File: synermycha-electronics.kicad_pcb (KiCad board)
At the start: 4 copper layers, 50 x 75 mm, 159 parts, among them J1 BATT, J11 USB_B_Micro, J12 Conn_01x05, J13 Conn_01x05, J14 Conn_01x05, J15 Conn_01x05, J16 Conn_01x05, J17 Conn_01x03, J2 Conn_01x02, J3 Conn_01x02, J4 USB_B_Micro, J5 ESP_01, J6 A1250WV-S-4P, Q1 IRLML9301TRPBF, Q2 BC847, Q3 BC847, Q4 BC847, Q5 IRLML2060TRPBF, Q6 IRLML2060TRPBF, Q7 IRLML9301TRPBF, SW1 DTSM32N, SW2 DTSM32N, SW3 DTSM32N, SW4 DTSM32N, U1 LM1117LDX, U12 MPU-9250, U13 STM32F446RETx, U14 STM14_SW, U2 LM1117LDX, U3 LM1117LDX, U4 DRV8835, U5 LM1117LDX, U8 CP2102N-A01-GQFN28, U9 TS5A3167DBVR, Y1 16Mhz, 8pF

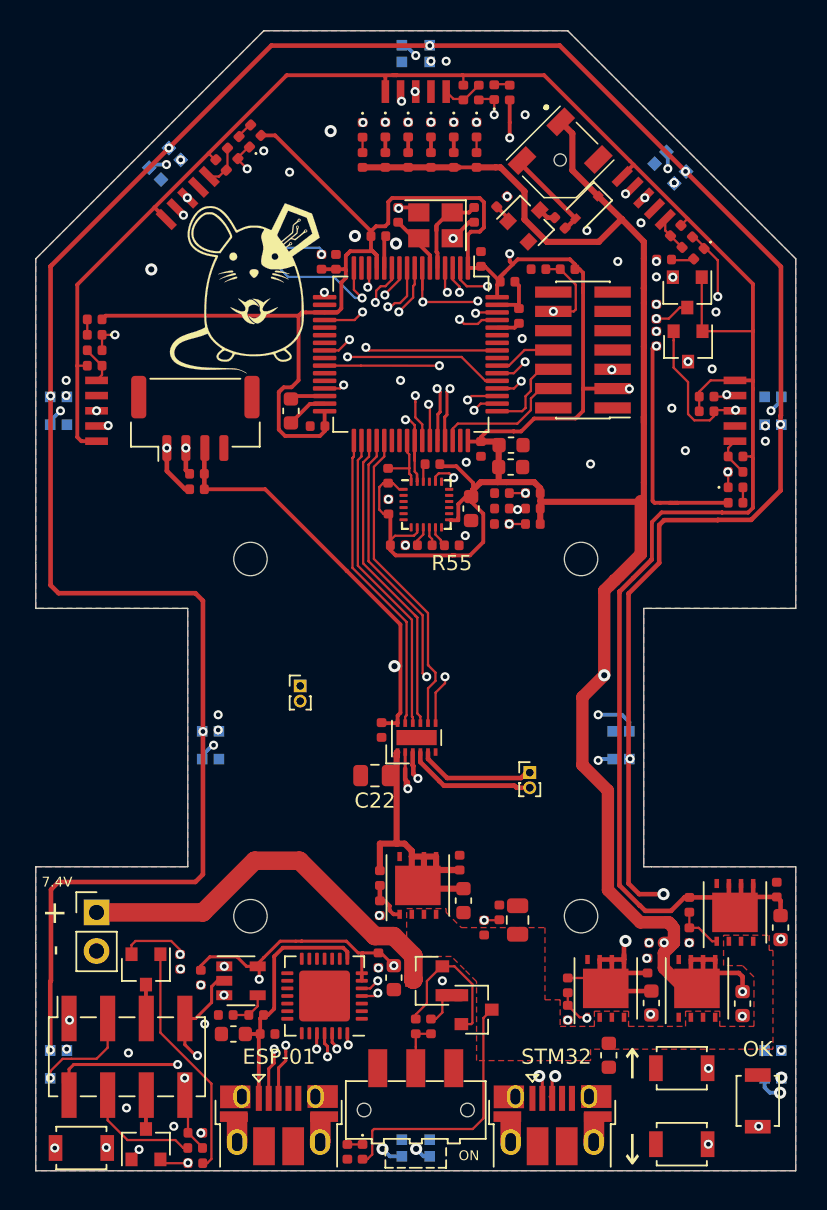
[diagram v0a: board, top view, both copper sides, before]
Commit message: Changes in graphics, added capacitors, changes in xshut
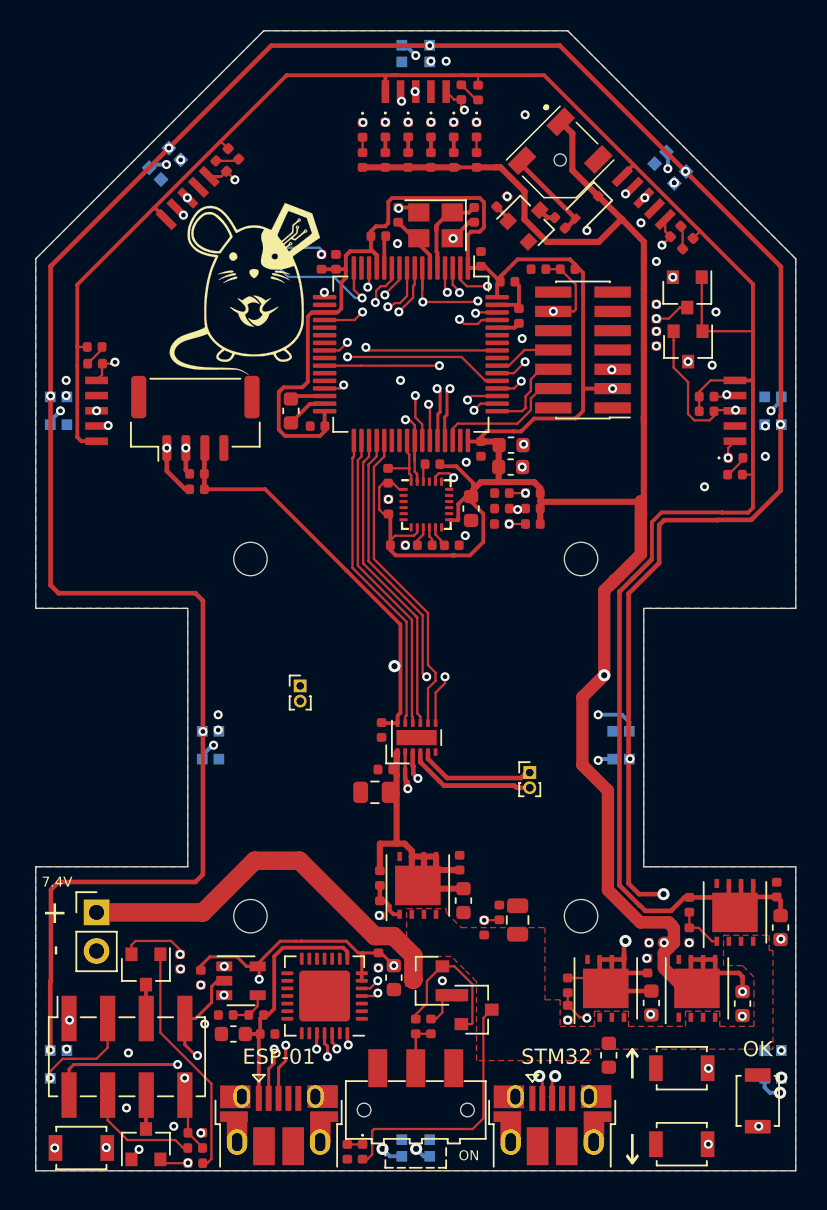
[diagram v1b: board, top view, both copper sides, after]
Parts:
- removed R36, R37, R38, R39, R40, R47, R48: 1K, Resistor_SMD:R_0402_1005Metric
- removed R41, R44, R45: 47K, Resistor_SMD:R_0402_1005Metric
- removed the REF** at (27.8, 137.8)
- added C23: 0.1uF, Capacitor_SMD:C_0402_1005Metric, F.Cu at (35.0, 171.6)
- R42, R43: value 47K -> 140R
- R46, R49, R50: value 1K -> 140R
- moved D18 2.20 mm to (24.2, 131.9)
- moved D15 2.16 mm to (40.0, 127.0)
- moved R49 2.15 mm to (25.0, 131.1), turned to 135 degrees
- moved D19 2.12 mm to (54.1, 136.2), turned to 45 degrees
- moved R46 2.08 mm to (41.1, 127.1), turned to 90 degrees
- moved D16 1.94 mm to (58.0, 151.1)
- moved D17 1.90 mm to (15.9, 144.9)
- moved R50 1.88 mm to (54.9, 137.0), turned to 45 degrees
- moved R43 1.23 mm to (15.9, 143.8)
- moved R42 1.20 mm to (58.0, 152.2)
- moved C22 1.10 mm to (34.3, 173.1)
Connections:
- D15 pad 1: Net-(D15-Pad1) -> /Distance Sensors/VL53L0x_~XSHUT[1]
- D16 pad 1: Net-(D16-Pad1) -> /Distance Sensors/VL53L0x_~XSHUT[2]
- D17 pad 1: Net-(D17-Pad1) -> /Distance Sensors/VL53L0x_~XSHUT[3]
- D18 pad 1: Net-(D18-Pad1) -> /Distance Sensors/VL53L0x_~XSHUT[4]
- D19 pad 1: Net-(D19-Pad1) -> /Distance Sensors/VL53L0x_~XSHUT[5]
- R42 pad 2: /Distance Sensors/VL53L0x_~XSHUT[2] -> Net-(D16-Pad2)
- R43 pad 2: /Distance Sensors/VL53L0x_~XSHUT[3] -> Net-(D17-Pad2)
- R46 pad 2: +3V3 -> +2V8
- R49 pad 2: +3V3 -> +2V8
- R50 pad 2: +3V3 -> +2V8
- U13 pad 2: Net-(D19-Pad1) -> /Distance Sensors/VL53L0x_~XSHUT[5]
- U13 pad 20: Net-(D18-Pad1) -> /Distance Sensors/VL53L0x_~XSHUT[4]
- U13 pad 24: Net-(D17-Pad1) -> /Distance Sensors/VL53L0x_~XSHUT[3]
- U13 pad 3: Net-(D15-Pad1) -> /Distance Sensors/VL53L0x_~XSHUT[1]
- U13 pad 54: Net-(D16-Pad1) -> /Distance Sensors/VL53L0x_~XSHUT[2]
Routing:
- net +3V3: track 391.5 -> 341.8 mm, vias 13 -> 11
- net Net-(D19-Pad1): track 23.0 -> 0.00 mm, vias 2 -> 0
- net Net-(D16-Pad1): track 20.8 -> 0.00 mm, vias 2 -> 0
- net /Distance Sensors/VL53L0x_~XSHUT[4]: track 2.82 -> 22.4 mm, vias 0 -> 2
- net Net-(D17-Pad1): track 19.4 -> 0.00 mm, vias 2 -> 0
- net Net-(D18-Pad1): track 19.1 -> 0.00 mm, vias 2 -> 0
- net /Distance Sensors/VL53L0x_~XSHUT[2]: track 3.16 -> 20.6 mm, vias 0 -> 2
- net /Distance Sensors/VL53L0x_~XSHUT[3]: track 3.06 -> 20.1 mm, vias 0 -> 2
- net Net-(D15-Pad1): track 16.5 -> 0.00 mm, vias 2 -> 0
- net /Distance Sensors/VL53L0x_~XSHUT[5]: track 2.42 -> 17.4 mm, vias 0 -> 2
- net /Distance Sensors/VL53L0x_~XSHUT[1]: track 2.80 -> 17.6 mm, vias 0 -> 2
- net +6V: track 27.0 -> 27.6 mm
- net Net-(D16-Pad2): track 1.02 -> 1.55 mm
- net GND: vias 48 -> 41

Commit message: Cosmetics update
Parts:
- added REF**: mocowanie_silników, mocowanie_silników:mocowanie_silników, F.Cu at (36.9, 168.5)
- moved R5 0.56 mm to (55.5, 180.8)
- moved R6 0.50 mm to (55.5, 182.5)
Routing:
- net +3V3: track 341.8 -> 328.7 mm, vias 11 -> 10
- net Net-(J3-Pad2): track 17.8 -> 13.2 mm
- net +5V: track 255.4 -> 258.2 mm
- net /Distance Sensors/VL53L0x_~XSHUT[1]: track 17.6 -> 18.3 mm
- net Net-(R5-Pad2): track 3.20 -> 2.58 mm
- net +2V8: track 154.7 -> 155.3 mm
- net GND: vias 41 -> 40
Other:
- outline, holes or cut-outs redrawn

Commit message: Estetics
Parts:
- added REF**: hole_0.8mm, holes:hole_0.8mm, F.Cu at (27.8, 137.8)
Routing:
- net +3V3: track 328.7 -> 338.5 mm, vias 10 -> 9
- net Net-(J3-Pad2): track 13.2 -> 17.8 mm
- net GND: track 14.8 -> 16.7 mm, vias 40 -> 38
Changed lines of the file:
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@@
   (general
     (thickness 1.6)
-    (drawings 50)
-    (tracks 1605)
+    (drawings 49)
+    (tracks 1610)
     (zones 0)
-    (modules 150)
+    (modules 151)
     (nets 105)
   )
@@
     (2 In2.Cu signal)
     (31 B.Cu signal)
-    (32 B.Adhes user)
-    (33 F.Adhes user)
-    (34 B.Paste user)
-    (35 F.Paste user)
+    (32 B.Adhes user hide)
+    (33 F.Adhes user hide)
+    (34 B.Paste user hide)
+    (35 F.Paste user hide)
     (36 B.SilkS user)
     (37 F.SilkS user)
@@
     (39 F.Mask user)
     (40 Dwgs.User user)
-    (41 Cmts.User user)
-    (42 Eco1.User user)
-    (43 Eco2.User user)
+    (41 Cmts.User user hide)
+    (42 Eco1.User user hide)
+    (43 Eco2.User user hide)
     (44 Edge.Cuts user)
-    (45 Margin user)
-    (46 B.CrtYd user)
-    (47 F.CrtYd user)
-    (48 B.Fab user)
-    (49 F.Fab user)
+    (45 Margin user hide)
+    (46 B.CrtYd user hide)
+    (47 F.CrtYd user hide)
+    (48 B.Fab user hide)
+    (49 F.Fab user hide)
   )
   (setup
-    (last_trace_width 0.25)
+    (last_trace_width 0.3048)
     (user_trace_width 0.1524)
     (user_trace_width 0.2032)
@@
     (add_net "Net-(R55-Pad2)")
   )
+  (module holes:hole_0.8mm (layer F.Cu)
+    (at 27.75 137.85)
+    (fp_text reference REF** (at 0 -2.5) (layer F.SilkS) hide
+      (effects (font (size 1 1) (thickness 0.15)))
+    )
+    (fp_text value hole_0.8mm (at 0 -0.5) (layer F.Fab)
+      (effects (font (size 1 1) (thickness 0.15)))
+    )
+    (pad "" np_thru_hole circle (at 0 0) (size 0.8 0.8) (drill 0.762) (layers *.Cu *.Mask))
+  )
   (module mocowanie_silników:mocowanie_silników (layer F.Cu)
     (at 36.9 168.5 180)
-    (fp_text reference REF** (at 16 5.75) (layer F.SilkS)
+    (fp_text reference REF** (at 16 5.75) (layer F.SilkS) hide
       (effects (font (size 1 1) (thickness 0.15)))
     )
@@
       (rotate (xyz -90 0 90))
     )
+    (model ${KIPRJMOD}/3D_models/FTSH-107-01-L-DV-K-TR.stp
+      (offset (xyz 0 0 0.5))
+      (scale (xyz 1 1 1))
+      (rotate (xyz -90 0 90))
+    )
   )
   (module Capacitor_SMD:C_0402_1005Metric (layer F.Cu)
@@
   (gr_arc (start 13 197) (end 12 197) (angle -90) (layer Edge.Cuts) (width 0.05))
   (gr_arc (start 61 197) (end 61 198) (angle -90) (layer Edge.Cuts) (width 0.05))
-  (dimension 75 (width 0.15) (layer Dwgs.User)
-    (gr_text "75,000 mm" (at -73.3 160.5 270) (layer Dwgs.User)
-      (effects (font (size 1 1) (thickness 0.15)))
-    )
-    (feature1 (pts (xy 38 198) (xy -72.586421 198)))
-    (feature2 (pts (xy 38 123) (xy -72.586421 123)))
-    (crossbar (pts (xy -72 123) (xy -72 198)))
-    (arrow1a (pts (xy -72 198) (xy -72.586421 196.873496)))
-    (arrow1b (pts (xy -72 198) (xy -71.413579 196.873496)))
-    (arrow2a (pts (xy -72 123) (xy -72.586421 124.126504)))
-    (arrow2b (pts (xy -72 123) (xy -71.413579 124.126504)))
-  )
   (dimension 17 (width 0.15) (layer Dwgs.User)
     (gr_text "17,000 mm" (at -11.3 169.5 90) (layer Dwgs.User)
@@
     (effects (font (size 0.65 0.65) (thickness 0.15)))
   )
-  (gr_text 7.4V (at 13.4 179) (layer F.SilkS)
+  (gr_text 7.4V (at 16 179) (layer F.SilkS)
     (effects (font (size 0.65 0.65) (thickness 0.15)))
   )
@@
   (via (at 52.451 187.706) (size 0.6) (drill 0.3) (layers F.Cu B.Cu) (net 1))
   (via (at 52.197 184.023) (size 0.6) (drill 0.3) (layers F.Cu B.Cu) (net 1))
-  (via (at 34.6 181.2) (size 0.6) (drill 0.3) (layers F.Cu B.Cu) (net 1))
   (via (at 47 188.085) (size 0.6) (drill 0.3) (layers F.Cu B.Cu) (net 1))
-  (via (at 34.544 184.658) (size 0.6) (drill 0.3) (layers F.Cu B.Cu) (net 1))
   (via (at 49.9 145.3) (size 0.6) (drill 0.3) (layers F.Cu B.Cu) (net 1))
   (via (at 24.384 186.436) (size 0.6) (drill 0.3) (layers F.Cu B.Cu) (net 1))
@@
   (via (at 44.196 128.524) (size 0.6) (drill 0.3) (layers F.Cu B.Cu) (net 1))
   (via (at 35.8 137) (size 0.6) (drill 0.3) (layers F.Cu B.Cu) (net 1))
+  (segment (start 34.544 184.664482) (end 34.544 184.635) (width 0.1524) (layer F.Cu) (net 1))
+  (segment (start 35.56 185.680482) (end 34.544 184.664482) (width 0.1524) (layer F.Cu) (net 1))
+  (segment (start 35.56 186.0805) (end 35.56 185.680482) (width 0.1524) (layer F.Cu) (net 1))
   (segment (start 38.338 177.326) (end 37.538 177.326) (width 0.4064) (layer F.Cu) (net 2))
   (segment (start 37.538 177.326) (end 36.738 177.326) (width 0.4064) (layer F.Cu) (net 2))
@@
   (segment (start 45.189 153.416) (end 45.189 153.096) (width 0.4064) (layer F.Cu) (net 3))
   (segment (start 35.56 184.5055) (end 35.56 184.5055) (width 0.2032) (layer F.Cu) (net 3))
-  (via (at 35.56 184.5055) (size 0.6) (drill 0.3) (layers F.Cu B.Cu) (net 3))
   (segment (start 52.0065 153.9875) (end 45.2755 153.9875) (width 0.4064) (layer F.Cu) (net 3))
   (segment (start 45.189 153.416) (end 45.212 153.924) (width 0.4064) (layer F.Cu) (net 3))
@@
   (segment (start 53.34 184.277) (end 53.34 183) (width 0.3048) (layer In1.Cu) (net 3))
   (segment (start 52.941599 184.675401) (end 53.34 184.277) (width 0.3048) (layer In1.Cu) (net 3))
-  (segment (start 35.704401 184.675401) (end 52.941599 184.675401) (width 0.3048) (layer In1.Cu) (net 3))
-  (segment (start 35.56 184.5055) (end 35.56 184.531) (width 0.3048) (layer In1.Cu) (net 3))
-  (segment (start 35.56 184.531) (end 35.704401 184.675401) (width 0.3048) (layer In1.Cu) (net 3))
   (segment (start 47.303201 132.178277) (end 49.002462 133.877538) (width 0.4064) (layer F.Cu) (net 3))
   (segment (start 46.535355 128.989771) (end 47.303201 129.757617) (width 0.4064) (layer F.Cu) (net 3))
@@
   (segment (start 53 181.211211) (end 51.322092 181.211211) (width 0.8128) (layer F.Cu) (net 3))
   (segment (start 53.317 181.528211) (end 53 181.211211) (width 0.8128) (layer F.Cu) (net 3))
+  (segment (start 27.424599 184.675401) (end 26.7 185.4) (width 0.3048) (layer In1.Cu) (net 3))
+  (segment (start 36.475401 184.675401) (end 27.424599 184.675401) (width 0.3048) (layer In1.Cu) (net 3))
+  (segment (start 36.475401 184.675401) (end 52.941599 184.675401) (width 0.3048) (layer In1.Cu) (net 3))
+  (segment (start 35.704401 184.675401) (end 36.475401 184.675401) (width 0.3048) (layer In1.Cu) (net 3))
   (segment (start 61 180.235) (end 60.75 179.985) (width 0.3048) (layer F.Cu) (net 4))
   (segment (start 61 181.2125) (end 61 180.235) (width 0.3048) (layer F.Cu) (net 4))
@@
   (segment (start 38.56039 172.370298) (end 37.30019 171.110099) (width 0.3048) (layer F.Cu) (net 20))
   (segment (start 38.856101 172.66601) (end 38.56039 172.370298) (width 0.3048) (layer F.Cu) (net 20))
+  (segment (start 38.844985 172.61521) (end 43.434 172.61521) (width 0.2032) (layer F.Cu) (net 20))
   (segment (start 44.5 171.8) (end 44.5 172.008) (width 0.3048) (layer F.Cu) (net 21))
   (segment (start 44.5 172.008) (end 44.485401 172.022599) (width 0.3048) (layer F.Cu) (net 21))
@@
   (segment (start 42.47 181.515) (end 42.5 181.485) (width 0.1524) (layer F.Cu) (net 30))
   (segment (start 41.5 181.515) (end 42.47 181.515) (width 0.1524) (layer F.Cu) (net 30))
-  (via (at 41.5 181.515) (size 0.6) (drill 0.3) (layers F.Cu B.Cu) (net 30))
   (segment (start 38.634 145.034) (end 38.5572 145.034) (width 0.1524) (layer In2.Cu) (net 30))
   (segment (start 39.829289 146.229289) (end 38.634 145.034) (width 0.1524) (layer In2.Cu) (net 30))
@@
   (segment (start 40.20121 166.449031) (end 41.80121 164.849031) (width 0.1524) (layer In2.Cu) (net 30))
   (segment (start 41.80121 149.750969) (end 39.829289 147.779049) (width 0.1524) (layer In2.Cu) (net 30))
-  (segment (start 41.5 181.515) (end 41.18 181.515) (width 0.1524) (layer In2.Cu) (net 30))
-  (segment (start 41.18 181.515) (end 40.20121 180.53621) (width 0.1524) (layer In2.Cu) (net 30))
-  (segment (start 40.20121 180.53621) (end 40.20121 166.449031) (width 0.1524) (layer In2.Cu) (net 30))
   (segment (start 41.80121 164.849031) (end 41.80121 149.750969) (width 0.1524) (layer In2.Cu) (net 30))
+  (via (at 40.425 173.40121) (size 0.6) (drill 0.3) (layers F.Cu B.Cu) (net 30))
+  (segment (start 41.5 181.515) (end 41.5 174.47621) (width 0.1524) (layer F.Cu) (net 30))
+  (segment (start 41.5 174.47621) (end 40.425 173.40121) (width 0.1524) (layer F.Cu) (net 30))
+  (segment (start 40.40121 173.40121) (end 40.20121 173.20121) (width 0.1524) (layer In2.Cu) (net 30))
+  (segment (start 40.425 173.40121) (end 40.40121 173.40121) (width 0.1524) (layer In2.Cu) (net 30))
+  (segment (start 40.20121 173.20121) (end 40.20121 173.19879) (width 0.1524) (layer In2.Cu) (net 30))
+  (segment (start 40.20121 173.19879) (end 40.20121 166.449031) (width 0.1524) (layer In2.Cu) (net 30))
   (segment (start 34.638 179.226) (end 34.638 180.241) (width 0.3048) (layer F.Cu) (net 31))
   (segment (start 35.28501 180.56801) (end 34.958 180.241) (width 0.254) (layer F.Cu) (net 31))
